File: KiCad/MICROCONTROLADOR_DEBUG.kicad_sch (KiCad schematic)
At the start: 8 parts, among them U1 PIC24HJ128GP504-I_PT, Y1 8MHz

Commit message: Routing V3
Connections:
- net OSC_-: now reaches C_OSC2.1, Y1.2
- net OSC_-: now also U1.30 (OSC1/CLKI/CN30/RA2); no longer U1.31 (OSC2/CLKO/CN29/RA3)
- net OSC_+: now reaches C_OSC1.1, Y1.1
- net OSC_+: now also U1.31 (OSC2/CLKO/CN29/RA3); no longer U1.30 (OSC1/CLKI/CN30/RA2)
- no-connect marks 7 -> 6
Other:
- moved on the sheet: C_OSC1, C_OSC2, Y1
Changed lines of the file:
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@@
 	)
 	(junction
-		(at 54.61 87.63)
+		(at 31.75 93.98)
 		(diameter 0)
 		(color 0 0 0 0)
 	)
 	(junction
-		(at 71.12 87.63)
+		(at 48.26 93.98)
 		(diameter 0)
 		(color 0 0 0 0)
@@
 	)
 	(no_connect
-		(at 104.14 73.66)
-	)
-	(no_connect
 		(at 104.14 121.92)
 	)
@@
 	(wire
 		(pts
-			(xy 71.12 78.74) (xy 71.12 87.63)
-		)
-		(stroke
-			(width 0)
-			(type default)
-		)
-	)
-	(wire
-		(pts
 			(xy 60.96 40.64) (xy 63.5 40.64)
 		)
@@
 	(wire
 		(pts
-			(xy 71.12 87.63) (xy 71.12 90.17)
+			(xy 48.26 93.98) (xy 48.26 96.52)
 		)
 		(stroke
@@
 	(wire
 		(pts
-			(xy 54.61 87.63) (xy 54.61 90.17)
+			(xy 31.75 93.98) (xy 31.75 96.52)
+		)
+		(stroke
+			(width 0)
+			(type default)
+		)
+	)
+	(wire
+		(pts
+			(xy 48.26 82.55) (xy 48.26 93.98)
 		)
 		(stroke
@@
 	(wire
 		(pts
-			(xy 54.61 76.2) (xy 54.61 87.63)
+			(xy 31.75 82.55) (xy 31.75 93.98)
 		)
 		(stroke
@@
 	(wire
 		(pts
-			(xy 54.61 87.63) (xy 59.69 87.63)
-		)
-		(stroke
-			(width 0)
-			(type default)
-		)
-	)
-	(wire
-		(pts
-			(xy 67.31 87.63) (xy 71.12 87.63)
+			(xy 31.75 93.98) (xy 36.83 93.98)
+		)
+		(stroke
+			(width 0)
+			(type default)
+		)
+	)
+	(wire
+		(pts
+			(xy 44.45 93.98) (xy 48.26 93.98)
 		)
 		(stroke
@@
 		)
 	)
-	(wire
-		(pts
-			(xy 54.61 76.2) (xy 104.14 76.2)
-		)
-		(stroke
-			(width 0)
-			(type default)
-		)
-	)
-	(wire
-		(pts
-			(xy 71.12 78.74) (xy 104.14 78.74)
-		)
-		(stroke
-			(width 0)
-			(type default)
+	(global_label "OSC_-"
+		(shape input)
+		(at 48.26 82.55 90)
+		(fields_autoplaced yes)
+		(effects
+			(font
+				(size 1.27 1.27)
+			)
+			(justify left)
+		)
+		(property "Intersheetrefs" "${INTERSHEET_REFS}"
+			(at 48.26 73.2148 90)
+			(effects
+				(font
+					(size 1.27 1.27)
+				)
+				(justify left)
+				(hide yes)
+			)
+		)
+	)
+	(global_label "OSC_-"
+		(shape input)
+		(at 104.14 76.2 180)
+		(fields_autoplaced yes)
+		(effects
+			(font
+				(size 1.27 1.27)
+			)
+			(justify right)
+		)
+		(property "Intersheetrefs" "${INTERSHEET_REFS}"
+			(at 94.8048 76.2 0)
+			(effects
+				(font
+					(size 1.27 1.27)
+				)
+				(justify right)
+				(hide yes)
+			)
+		)
+	)
+	(global_label "OSC_+"
+		(shape input)
+		(at 31.75 82.55 90)
+		(fields_autoplaced yes)
+		(effects
+			(font
+				(size 1.27 1.27)
+			)
+			(justify left)
+		)
+		(property "Intersheetrefs" "${INTERSHEET_REFS}"
+			(at 31.75 73.2148 90)
+			(effects
+				(font
+					(size 1.27 1.27)
+				)
+				(justify left)
+				(hide yes)
+			)
+		)
+	)
+	(global_label "OSC_+"
+		(shape input)
+		(at 104.14 78.74 180)
+		(fields_autoplaced yes)
+		(effects
+			(font
+				(size 1.27 1.27)
+			)
+			(justify right)
+		)
+		(property "Intersheetrefs" "${INTERSHEET_REFS}"
+			(at 94.8048 78.74 0)
+			(effects
+				(font
+					(size 1.27 1.27)
+				)
+				(justify right)
+				(hide yes)
+			)
 		)
 	)
@@
 	(symbol
 		(lib_id "Device:C")
-		(at 71.12 93.98 0)
+		(at 48.26 100.33 0)
 		(unit 1)
 		(exclude_from_sim no)
@@
 		(fields_autoplaced yes)
 		(property "Reference" "C_OSC2"
-			(at 74.93 92.7099 0)
+			(at 52.07 99.0599 0)
 			(effects
 				(font
@@
 		)
 		(property "Value" "22pF"
-			(at 74.93 95.2499 0)
+			(at 52.07 101.5999 0)
 			(effects
 				(font
@@
 		)
 		(property "Footprint" "Capacitor_SMD:C_0603_1608Metric"
-			(at 72.0852 97.79 0)
+			(at 49.2252 104.14 0)
 			(effects
 				(font
@@
 		)
 		(property "Datasheet" "~"
-			(at 71.12 93.98 0)
+			(at 48.26 100.33 0)
 			(effects
 				(font
@@
 		)
 		(property "Description" "Unpolarized capacitor"
-			(at 71.12 93.98 0)
+			(at 48.26 100.33 0)
 			(effects
 				(font
@@
 	(symbol
 		(lib_id "Device:Crystal")
-		(at 63.5 87.63 0)
+		(at 40.64 93.98 0)
 		(unit 1)
 		(exclude_from_sim no)
@@
 		(fields_autoplaced yes)
 		(property "Reference" "Y1"
-			(at 63.5 80.01 0)
+			(at 40.64 86.36 0)
 			(effects
 				(font
@@
 		)
 		(property "Value" "8MHz"
-			(at 63.5 82.55 0)
+			(at 40.64 88.9 0)
 			(effects
 				(font
@@
 		)
 		(property "Footprint" "Crystal:Crystal_SMD_3225-4Pin_3.2x2.5mm"
-			(at 63.5 87.63 0)
+			(at 40.64 93.98 0)
 			(effects
 				(font
@@
 		)
 		(property "Datasheet" "~"
-			(at 63.5 87.63 0)
+			(at 40.64 93.98 0)
 			(effects
 				(font
@@
 		)
 		(property "Description" "Two pin crystal"
-			(at 63.5 87.63 0)
+			(at 40.64 93.98 0)
 			(effects
 				(font
@@
 	(symbol
 		(lib_id "power:GND")
-		(at 71.12 97.79 0)
+		(at 48.26 104.14 0)
 		(unit 1)
 		(exclude_from_sim no)
@@
 		(fields_autoplaced yes)
 		(property "Reference" "#PWR09"
-			(at 71.12 104.14 0)
+			(at 48.26 110.49 0)
 			(effects
 				(font
@@
 		)
 		(property "Value" "GND"
-			(at 71.12 102.87 0)
+			(at 48.26 109.22 0)
 			(effects
 				(font
@@
 		)
 		(property "Footprint" ""
-			(at 71.12 97.79 0)
+			(at 48.26 104.14 0)
 			(effects
 				(font
@@
 		)
 		(property "Datasheet" ""
-			(at 71.12 97.79 0)
+			(at 48.26 104.14 0)
 			(effects
 				(font
@@
 		)
 		(property "Description" "Power symbol creates a global label with name \"GND\" , ground"
-			(at 71.12 97.79 0)
+			(at 48.26 104.14 0)
 			(effects
 				(font
@@
 	(symbol
 		(lib_id "Device:C")
-		(at 54.61 93.98 0)
+		(at 31.75 100.33 0)
 		(unit 1)
 		(exclude_from_sim no)
@@
 		(fields_autoplaced yes)
 		(property "Reference" "C_OSC1"
-			(at 58.42 92.7099 0)
+			(at 35.56 99.0599 0)
 			(effects
 				(font
@@
 		)
 		(property "Value" "22pF"
-			(at 58.42 95.2499 0)
+			(at 35.56 101.5999 0)
 			(effects
 				(font
@@
 		)
 		(property "Footprint" "Capacitor_SMD:C_0603_1608Metric"
-			(at 55.5752 97.79 0)
+			(at 32.7152 104.14 0)
 			(effects
 				(font
@@
 		)
 		(property "Datasheet" "~"
-			(at 54.61 93.98 0)
+			(at 31.75 100.33 0)
 			(effects
 				(font
@@
 		)
 		(property "Description" "Unpolarized capacitor"
-			(at 54.61 93.98 0)
+			(at 31.75 100.33 0)
 			(effects
 				(font
@@
 	(symbol
 		(lib_id "power:GND")
-		(at 54.61 97.79 0)
+		(at 31.75 104.14 0)
 		(unit 1)
 		(exclude_from_sim no)
@@
 		(fields_autoplaced yes)
 		(property "Reference" "#PWR07"
-			(at 54.61 104.14 0)
+			(at 31.75 110.49 0)
 			(effects
 				(font
@@
 		)
 		(property "Value" "GND"
-			(at 54.61 102.87 0)
+			(at 31.75 109.22 0)
 			(effects
 				(font
@@
 		)
 		(property "Footprint" ""
-			(at 54.61 97.79 0)
+			(at 31.75 104.14 0)
 			(effects
 				(font
@@
 		)
 		(property "Datasheet" ""
-			(at 54.61 97.79 0)
+			(at 31.75 104.14 0)
 			(effects
 				(font
@@
 		)
 		(property "Description" "Power symbol creates a global label with name \"GND\" , ground"
-			(at 54.61 97.79 0)
-			(effects
-				(font
+			(at 31.75 104.14 0)
+			(effects
+				(font

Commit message: Versió preliminar Routing Final
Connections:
- net CAN_RX: now also U1.9 (PGEC2/RP11(1)/CN15/PMD1/RB11); no longer U1.4 (RP24(1)/CN20/PMA5/RC8)
- net CAN_TX: now also U1.10 (AN12/RP12(1)/CN14/PMD0/RB12); no longer U1.5 (RP25(1)/CN19/PMA6/RC9)
- net OSC_+: now also U1.30 (OSC1/CLKI/CN30/RA2); no longer U1.31 (OSC2/CLKO/CN29/RA3)
- net OSC_-: now also U1.31 (OSC2/CLKO/CN29/RA3); no longer U1.30 (OSC1/CLKI/CN30/RA2)
- no-connect marks 6 -> 7
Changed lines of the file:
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@@
+	)
+	(no_connect
+		(at 220.98 76.2)
 	)
 	(no_connect
@@
 	)
 	(no_connect
-		(at 104.14 127)
-	)
-	(no_connect
 		(at 104.14 88.9)
 	)
@@
 	)
 	(no_connect
-		(at 104.14 124.46)
+		(at 104.14 73.66)
+	)
+	(no_connect
+		(at 220.98 73.66)
 	)
 	(wire
@@
 	(global_label "OSC_-"
 		(shape input)
+		(at 104.14 78.74 180)
+		(fields_autoplaced yes)
+		(effects
+			(font
+				(size 1.27 1.27)
+			)
+			(justify right)
+		)
+		(property "Intersheetrefs" "${INTERSHEET_REFS}"
+			(at 94.8048 78.74 0)
+			(effects
+				(font
+					(size 1.27 1.27)
+				)
+				(justify right)
+				(hide yes)
+			)
+		)
+	)
+	(global_label "OSC_+"
+		(shape input)
+		(at 31.75 82.55 90)
+		(fields_autoplaced yes)
+		(effects
+			(font
+				(size 1.27 1.27)
+			)
+			(justify left)
+		)
+		(property "Intersheetrefs" "${INTERSHEET_REFS}"
+			(at 31.75 73.2148 90)
+			(effects
+				(font
+					(size 1.27 1.27)
+				)
+				(justify left)
+				(hide yes)
+			)
+		)
+	)
+	(global_label "OSC_+"
+		(shape input)
 		(at 104.14 76.2 180)
 		(fields_autoplaced yes)
@@
 		)
 	)
-	(global_label "OSC_+"
-		(shape input)
-		(at 31.75 82.55 90)
-		(fields_autoplaced yes)
-		(effects
-			(font
-				(size 1.27 1.27)
-			)
-			(justify left)
-		)
-		(property "Intersheetrefs" "${INTERSHEET_REFS}"
-			(at 31.75 73.2148 90)
-			(effects
-				(font
-					(size 1.27 1.27)
-				)
-				(justify left)
-				(hide yes)
-			)
-		)
-	)
-	(global_label "OSC_+"
-		(shape input)
-		(at 104.14 78.74 180)
-		(fields_autoplaced yes)
-		(effects
-			(font
-				(size 1.27 1.27)
-			)
-			(justify right)
-		)
-		(property "Intersheetrefs" "${INTERSHEET_REFS}"
-			(at 94.8048 78.74 0)
-			(effects
-				(font
-					(size 1.27 1.27)
-				)
-				(justify right)
-				(hide yes)
-			)
-		)
-	)
 	(hierarchical_label "WIN_BTN_UP"
 		(shape input)
@@
 	(hierarchical_label "CAN_RX"
 		(shape input)
-		(at 220.98 73.66 0)
-		(effects
-			(font
-				(size 1.27 1.27)
-			)
-			(justify left)
+		(at 104.14 124.46 180)
+		(effects
+			(font
+				(size 1.27 1.27)
+			)
+			(justify right)
 		)
 	)
@@
 	(hierarchical_label "CAN_TX"
 		(shape output)
-		(at 220.98 76.2 0)
-		(effects
-			(font
-				(size 1.27 1.27)
-			)
-			(justify left)
-		)
-	)
+		(at 104.14 127 180)
+		(effects
+			(font
+				(size 1.27 1.27)
+			)
+			(justify right)
+		)
+	)

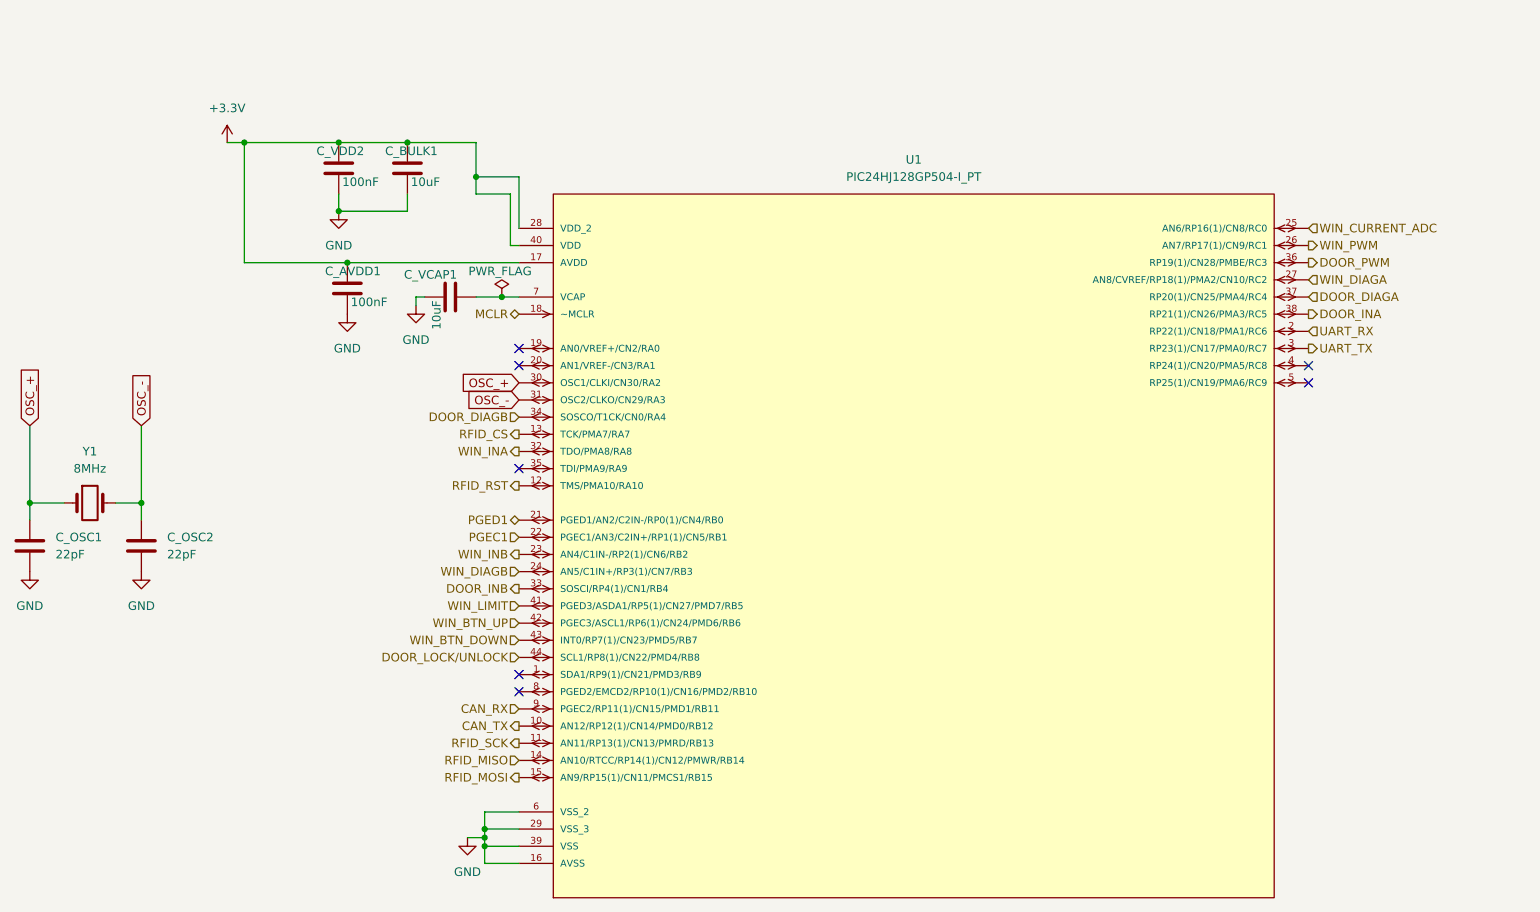
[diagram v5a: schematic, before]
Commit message: Actualització dels test points
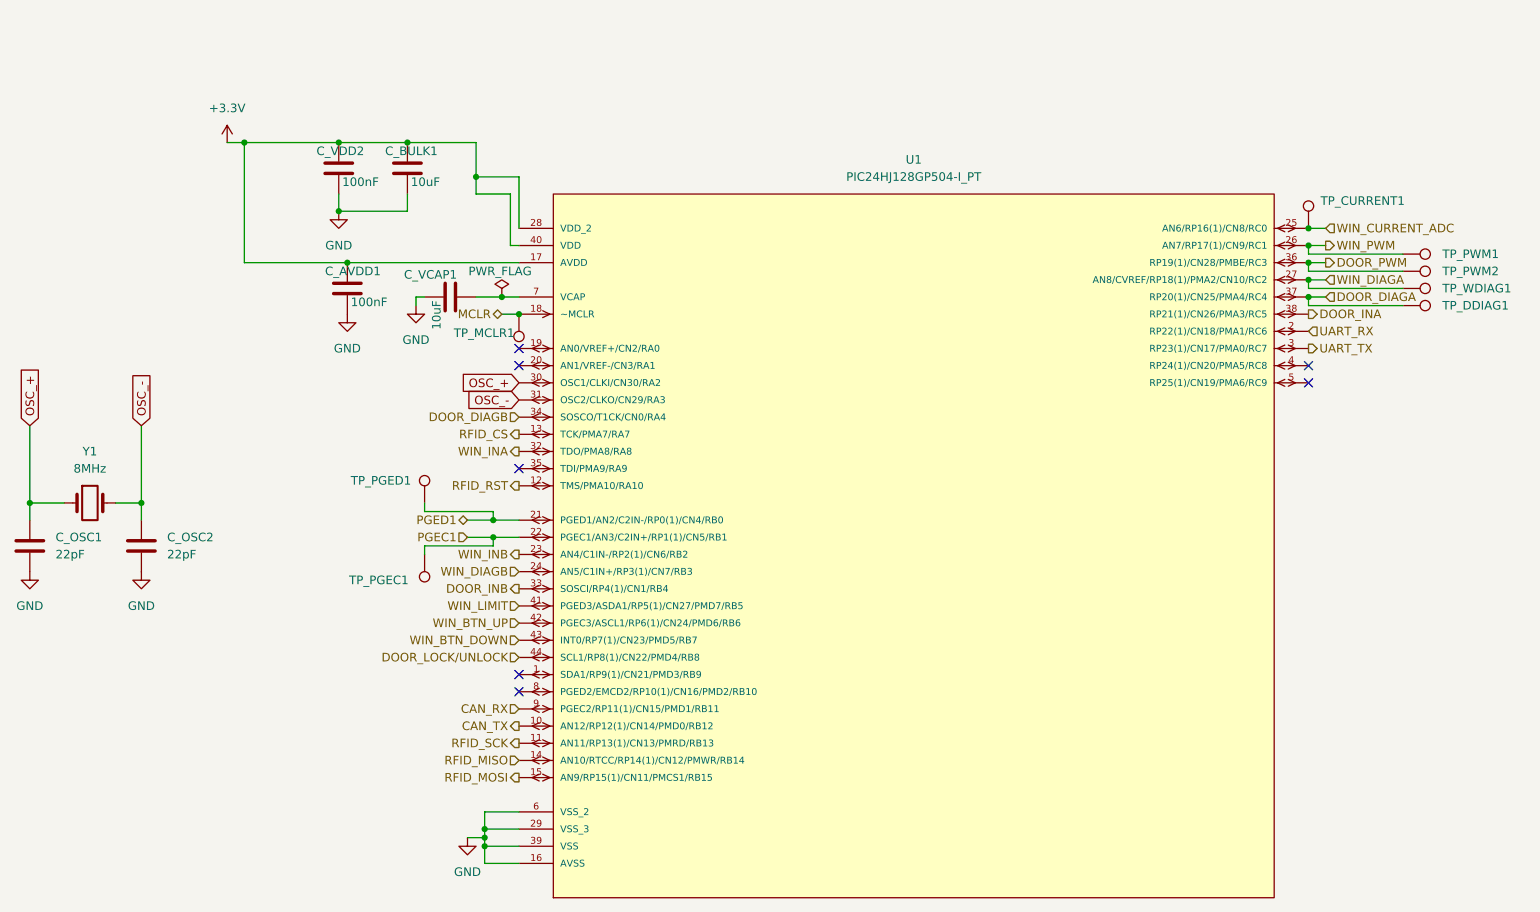
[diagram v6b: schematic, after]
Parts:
- added TP_CURRENT1, TP_DDIAG1, TP_MCLR1, TP_PGEC1, TP_PGED1, TP_PWM1, TP_PWM2, TP_WDIAG1: ~, TestPoint:TestPoint_Pad_D1.5mm, symbol Connector:TestPoint
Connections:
- net DOOR_DIAGA: now also TP_DDIAG1.1
- net DOOR_PWM: now also TP_PWM2.1
- net MCLR: now also TP_MCLR1.1
- net PGEC1: now also TP_PGEC1.1
- net PGED1: now also TP_PGED1.1
- net WIN_CURRENT_ADC: now also TP_CURRENT1.1
- net WIN_DIAGA: now also TP_WDIAG1.1
- net WIN_PWM: now also TP_PWM1.1

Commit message: Versio final
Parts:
- C_OSC1, C_OSC2: footprint Capacitor_SMD:C_0603_1608Metric -> Capacitor_SMD:C_0805_2012Metric
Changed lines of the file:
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@@
 			)
 		)
-		(property "Footprint" "Capacitor_SMD:C_0603_1608Metric"
+		(property "Footprint" "Capacitor_SMD:C_0805_2012Metric"
 			(at 49.2252 104.14 0)
 			(effects
@@
 			)
 		)
-		(property "Footprint" "Capacitor_SMD:C_0603_1608Metric"
+		(property "Footprint" "Capacitor_SMD:C_0805_2012Metric"
 			(at 32.7152 104.14 0)
 			(effects

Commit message: Versió Final projecte
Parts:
- C1: renamed from C_OSC1; footprint Capacitor_SMD:C_0805_2012Metric -> Capacitor_SMD:C_0603_1608Metric
- C2: renamed from C_OSC2; footprint Capacitor_SMD:C_0805_2012Metric -> Capacitor_SMD:C_0603_1608Metric
- renumbered C_VDD2 to C3, C_AVDD1 to C4, C_BULK1 to C5, C_VCAP1 to C6
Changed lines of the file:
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@@
 		(on_board yes)
 		(dnp no)
-		(property "Reference" "C_AVDD1"
+		(property "Reference" "C4"
 			(at 75.438 59.69 0)
 			(effects
@@
 			(project "PROJECTE_EINES"
 				(path "/347831db-5db9-4aff-ad32-e56fd770e219/1f039355-d395-4709-b940-eff82ebe0f62"
-					(reference "C_AVDD1")
+					(reference "C4")
 					(unit 1)
 				)
@@
 		(dnp no)
 		(fields_autoplaced yes)
-		(property "Reference" "#PWR08"
+		(property "Reference" "#PWR09"
 			(at 60.96 44.45 0)
 			(effects
@@
 			(project ""
 				(path "/347831db-5db9-4aff-ad32-e56fd770e219/1f039355-d395-4709-b940-eff82ebe0f62"
-					(reference "#PWR08")
+					(reference "#PWR09")
 					(unit 1)
 				)
@@
 		(dnp no)
 		(fields_autoplaced yes)
-		(property "Reference" "C_OSC2"
+		(property "Reference" "C2"
 			(at 52.07 99.0599 0)
 			(effects
@@
 			)
 		)
-		(property "Footprint" "Capacitor_SMD:C_0805_2012Metric"
+		(property "Footprint" "Capacitor_SMD:C_0603_1608Metric"
 			(at 49.2252 104.14 0)
 			(effects
@@
 			(project "PROJECTE_EINES"
 				(path "/347831db-5db9-4aff-ad32-e56fd770e219/1f039355-d395-4709-b940-eff82ebe0f62"
-					(reference "C_OSC2")
+					(reference "C2")
 					(unit 1)
 				)
@@
 		(dnp no)
 		(fields_autoplaced yes)
-		(property "Reference" "#PWR09"
+		(property "Reference" "#PWR08"
 			(at 48.26 110.49 0)
 			(effects
@@
 			(project "PROJECTE_EINES"
 				(path "/347831db-5db9-4aff-ad32-e56fd770e219/1f039355-d395-4709-b940-eff82ebe0f62"
-					(reference "#PWR09")
+					(reference "#PWR08")
 					(unit 1)
 				)
@@
 		(on_board yes)
 		(dnp no)
-		(property "Reference" "#FLG02"
+		(property "Reference" "#FLG03"
 			(at 101.6 61.595 0)
 			(effects
@@
 			(project ""
 				(path "/347831db-5db9-4aff-ad32-e56fd770e219/1f039355-d395-4709-b940-eff82ebe0f62"
-					(reference "#FLG02")
+					(reference "#FLG03")
 					(unit 1)
 				)
@@
 		(dnp no)
 		(fields_autoplaced yes)
-		(property "Reference" "C_OSC1"
+		(property "Reference" "C1"
 			(at 35.56 99.0599 0)
 			(effects
@@
 			)
 		)
-		(property "Footprint" "Capacitor_SMD:C_0805_2012Metric"
+		(property "Footprint" "Capacitor_SMD:C_0603_1608Metric"
 			(at 32.7152 104.14 0)
 			(effects
@@
 			(project "PROJECTE_EINES"
 				(path "/347831db-5db9-4aff-ad32-e56fd770e219/1f039355-d395-4709-b940-eff82ebe0f62"
-					(reference "C_OSC1")
+					(reference "C1")
 					(unit 1)
 				)
@@
 		(on_board yes)
 		(dnp no)
-		(property "Reference" "C_BULK1"
+		(property "Reference" "C5"
 			(at 84.328 41.91 0)
 			(effects
@@
 			(project "PROJECTE_EINES"
 				(path "/347831db-5db9-4aff-ad32-e56fd770e219/1f039355-d395-4709-b940-eff82ebe0f62"
-					(reference "C_BULK1")
+					(reference "C5")
 					(unit 1)
 				)
@@
 		(on_board yes)
 		(dnp no)
-		(property "Reference" "C_VCAP1"
+		(property "Reference" "C6"
 			(at 87.122 60.198 90)
 			(effects
@@
 			(project "PROJECTE_EINES"
 				(path "/347831db-5db9-4aff-ad32-e56fd770e219/1f039355-d395-4709-b940-eff82ebe0f62"
-					(reference "C_VCAP1")
+					(reference "C6")
 					(unit 1)
 				)
@@
 		(on_board yes)
 		(dnp no)
-		(property "Reference" "C_VDD2"
+		(property "Reference" "C3"
 			(at 74.168 41.91 0)
 			(effects
@@
 			(project "PROJECTE_EINES"
 				(path "/347831db-5db9-4aff-ad32-e56fd770e219/1f039355-d395-4709-b940-eff82ebe0f62"
-					(reference "C_VDD2")
-					(unit 1)
-				)
+					(reference "C3")
+					(unit 1)
+				)
